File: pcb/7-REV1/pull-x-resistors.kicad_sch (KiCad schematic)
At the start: 15 parts, among them U6 TCA6416RTWT, U7 TCA6416RTWT

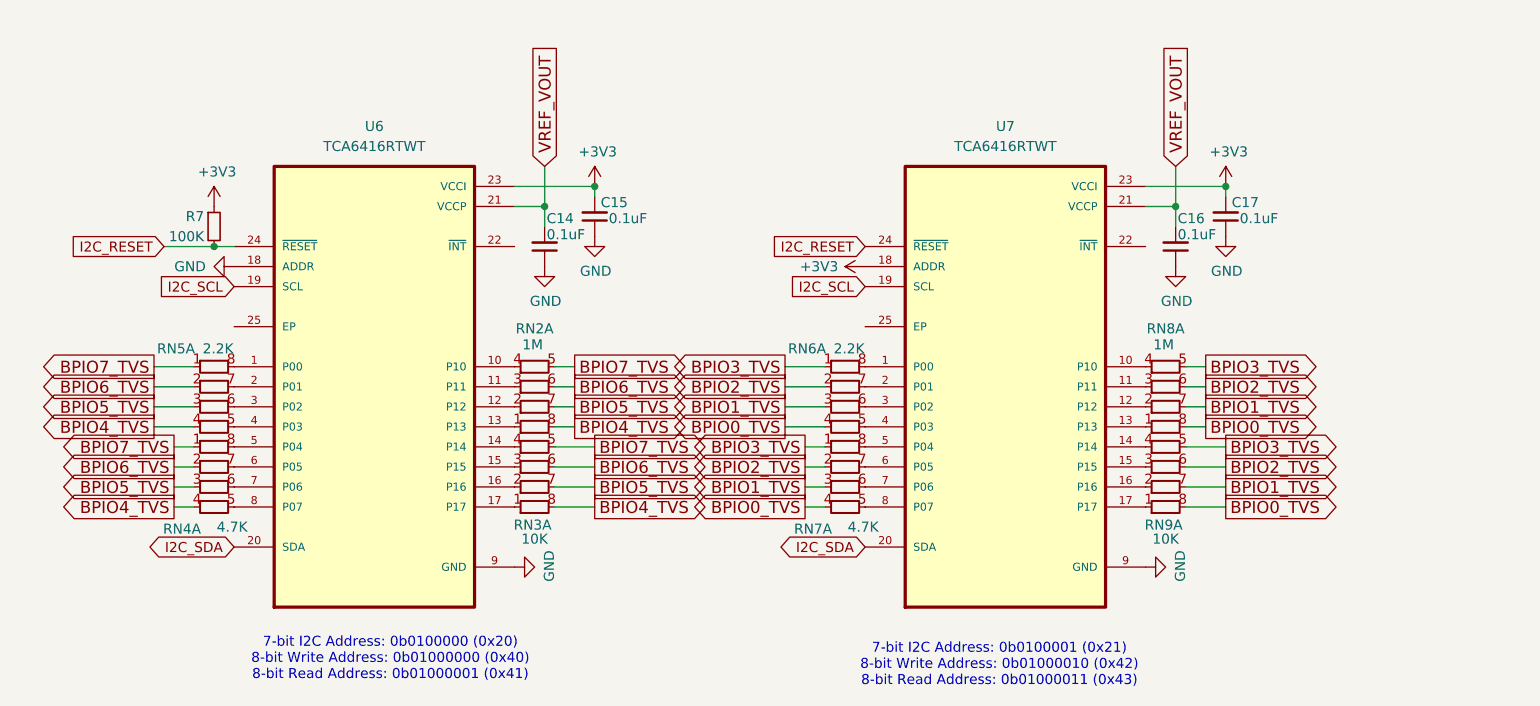
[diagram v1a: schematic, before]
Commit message: TCA6416ARTWR IO expander, 2.2uF->4.7uF
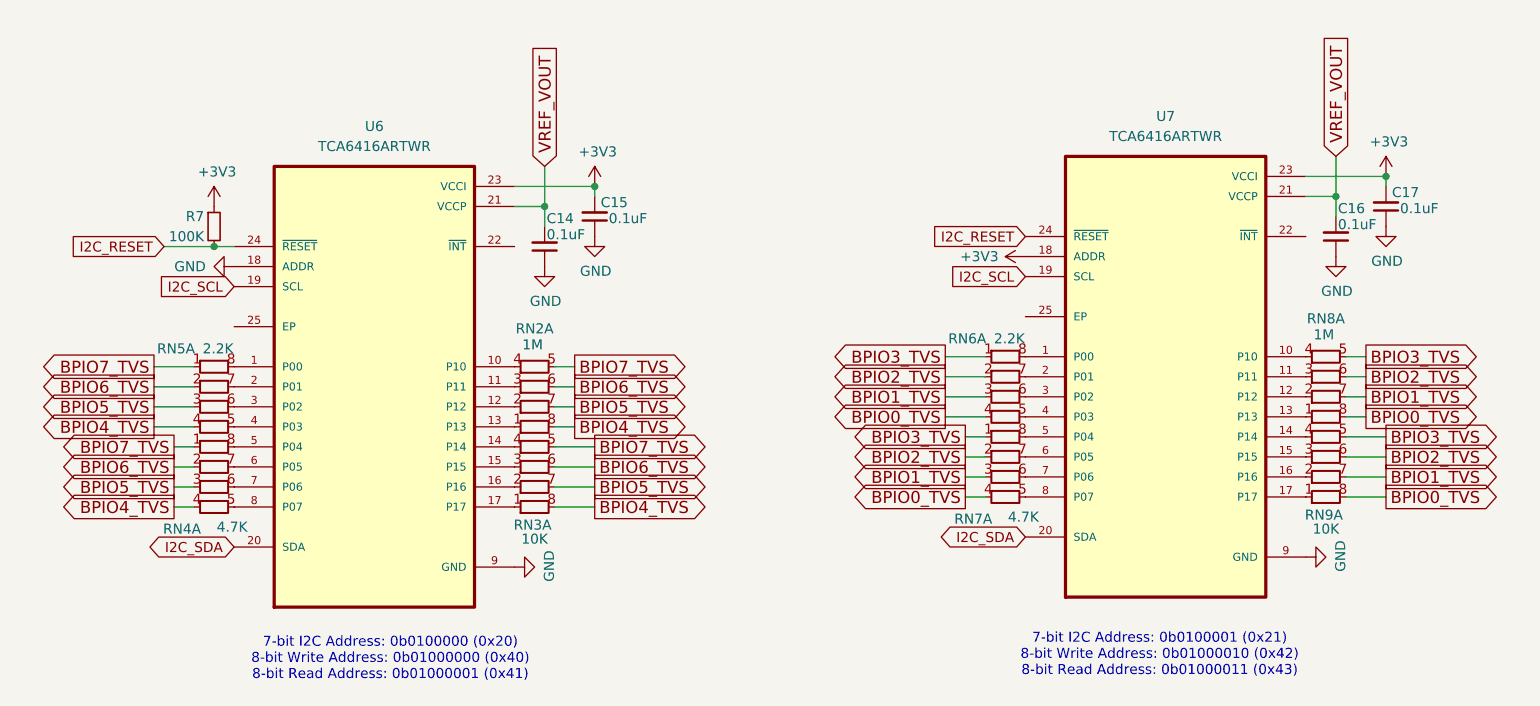
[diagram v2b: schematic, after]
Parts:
- U6, U7: value TCA6416RTWT -> TCA6416ARTWR
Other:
- moved on the sheet: C16, C17, RN6A, RN7A, RN8A, RN9A, U7

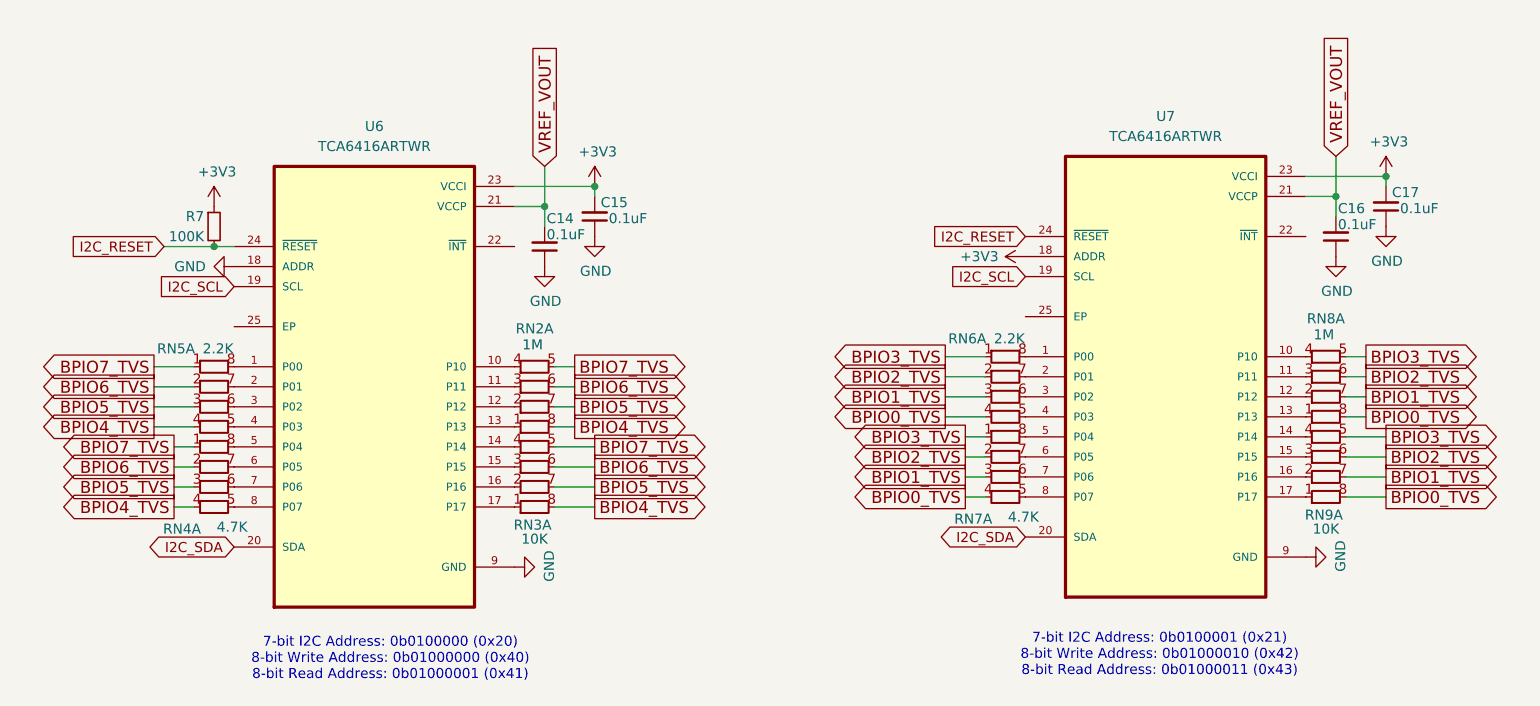
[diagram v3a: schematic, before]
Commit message: improve TCA6416ARTWR schematics - connect exposed pad to GND - mark unused INT pin as such
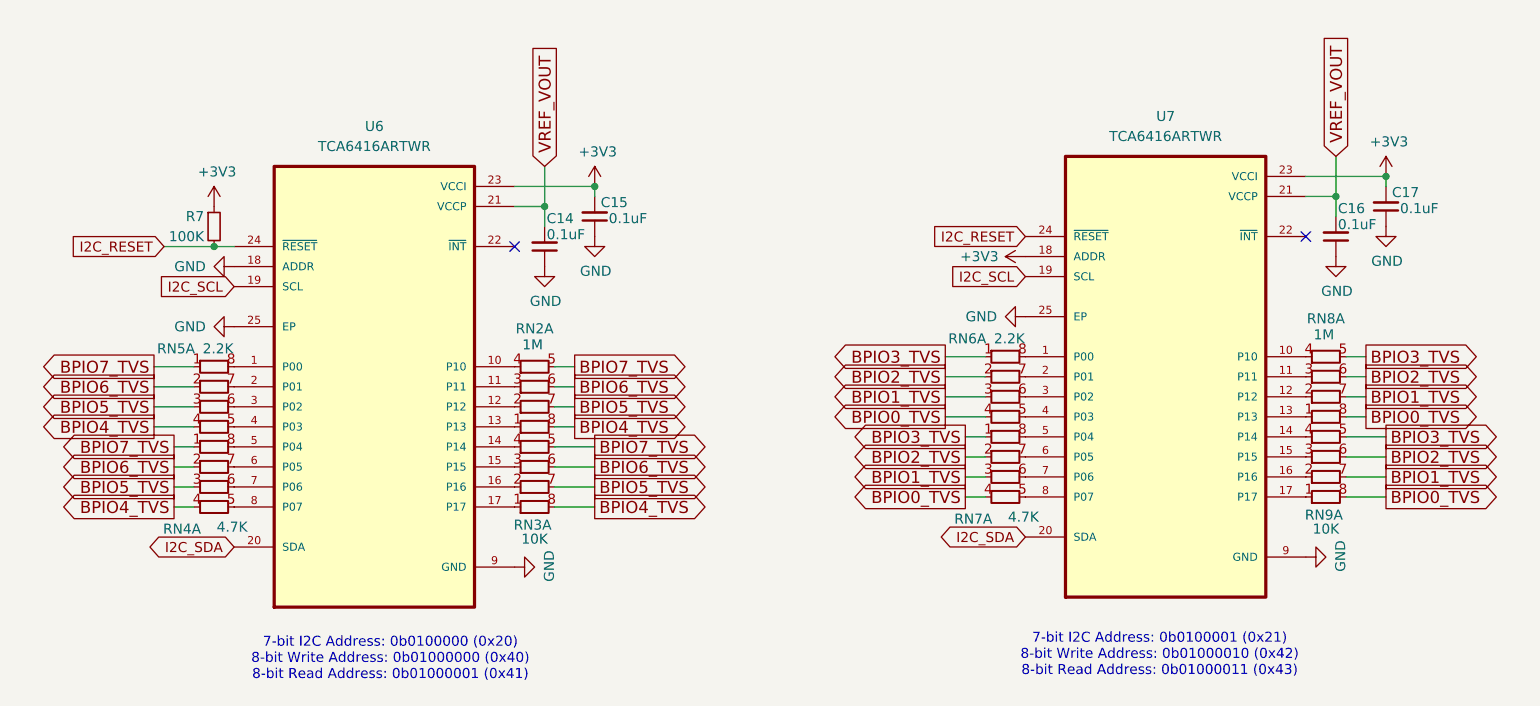
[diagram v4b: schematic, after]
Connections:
- net GND: now also U6.25 (EP), U7.25 (EP)
- no-connect marks 0 -> 2
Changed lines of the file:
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@@
 		(color 0 0 0 0)
 	)
+	(no_connect
+		(at 205.74 73.66)
+	)
+	(no_connect
+		(at 105.41 74.93)
+	)
 	(wire
 		(pts
@@
 	(symbol
 		(lib_id "power:GND")
+		(at 69.85 85.09 270)
+		(unit 1)
+		(exclude_from_sim no)
+		(in_bom yes)
+		(on_board yes)
+		(dnp no)
+		(property "Reference" "#PWR0150"
+			(at 63.5 85.09 0)
+			(effects
+				(font
+					(size 1.27 1.27)
+				)
+				(hide yes)
+			)
+		)
+		(property "Value" "GND"
+			(at 64.262 85.09 90)
+			(effects
+				(font
+					(size 1.27 1.27)
+				)
+			)
+		)
+		(property "Footprint" ""
+			(at 69.85 85.09 0)
+			(effects
+				(font
+					(size 1.27 1.27)
+				)
+				(hide yes)
+			)
+		)
+		(property "Datasheet" ""
+			(at 69.85 85.09 0)
+			(effects
+				(font
+					(size 1.27 1.27)
+				)
+				(hide yes)
+			)
+		)
+		(property "Description" ""
+			(at 69.85 85.09 0)
+			(effects
+				(font
+					(size 1.27 1.27)
+				)
+				(hide yes)
+			)
+		)
+		(pin "1"
+		)
+		(instances
+			(project "7-REV1"
+				(path "/1f56410a-eaac-4444-b0f7-cfd3531e22ac/70d89944-cef2-4c07-9520-6c47f8613415"
+					(reference "#PWR0150")
+					(unit 1)
+				)
+			)
+		)
+	)
+	(symbol
+		(lib_id "power:GND")
 		(at 215.9 72.39 0)
 		(unit 1)
@@
 					(unit 1)
 				)
+			)
+		)
+	)
+	(symbol
+		(lib_id "power:GND")
+		(at 170.18 83.82 270)
+		(unit 1)
+		(exclude_from_sim no)
+		(in_bom yes)
+		(on_board yes)
+		(dnp no)
+		(property "Reference" "#PWR0151"
+			(at 163.83 83.82 0)
+			(effects
+				(font
+					(size 1.27 1.27)
+				)
+				(hide yes)
+			)
+		)
+		(property "Value" "GND"
+			(at 164.592 83.82 90)
+			(effects
+				(font
+					(size 1.27 1.27)
+				)
+			)
+		)
+		(property "Footprint" ""
+			(at 170.18 83.82 0)
+			(effects
+				(font
+					(size 1.27 1.27)
+				)
+				(hide yes)
+			)
+		)
+		(property "Datasheet" ""
+			(at 170.18 83.82 0)
+			(effects
+				(font
+					(size 1.27 1.27)
+				)
+				(hide yes)
+			)
+		)
+		(property "Description" ""
+			(at 170.18 83.82 0)
+			(effects
+				(font
+					(size 1.27 1.27)
+				)
+				(hide yes)
+			)
+		)
+		(pin "1"
+		)
+		(instances
+			(project "7-REV1"
+				(path "/1f56410a-eaac-4444-b0f7-cfd3531e22ac/70d89944-cef2-4c07-9520-6c47f8613415"
+					(reference "#PWR0151")
+					(unit 1)
+				)
